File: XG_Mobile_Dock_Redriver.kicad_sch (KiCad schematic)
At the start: 141 parts, among them J1 5-1775443-8, J13 39301240, J14 I2C1, J2 20455-040E-76, J3 20455-040E-76, J5 USB_C_Receptacle, J6 455860005, J7 10147430-113T0LF, SW1 SW_Push, U1 DS320PR810NJXR, U2 DS320PR810NJXR, U6 AT24C02D-PUM

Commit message: stuff
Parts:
- removed R100, R104, R69, R73, R81, R88, R92, R96: 75k, Resistor_SMD:R_0603_1608Metric, symbol Device:R
- removed R102, R105, R108, R67, R71, R98: 8.25k, Resistor_SMD:R_0603_1608Metric, symbol Device:R
- removed R103, R68, R72, R80, R87, R91, R95, R99: 24.9k, Resistor_SMD:R_0603_1608Metric, symbol Device:R
- removed R107, R64, R78, R82, R89, R93: 1k, Resistor_SMD:R_0603_1608Metric, symbol Device:R
- removed R111, R112: 4.7k, Resistor_SMD:R_0402_1005Metric, symbol Device:R
- removed SW10, SW11, SW12, SW13, SW14, SW15, SW6, SW7: ~, DSWB04LHGET:SW-TH_DSWB04LHGET, symbol DSWB04LHGET:DSWB04LHGET
- removed SW16, SW17, SW18, SW19: ~, DSWB01LHGET:SW-TH_DSWB01LHGET, symbol DSWB01LHGET:DSWB01LHGET
- removed SW2, SW3: ~, DSWB03LHGET:SW-TH_DSWB03LHGET, symbol DSWB03LHGET:DSWB03LHGET
- removed U5: ~, DIP-8_L10.2-W10.2-P2.54-LS7.6-BL:DIP-8_L10.2-W10.2-P2.54-LS7.6-BL, symbol DS1009-08AT1NX-0A2:DS1009-08AT1NX-0A2
- removed U6: AT24C02D-PUM, AT24C02D-PUM:PDIP8_300MC_MCH, symbol AT24C02D-PUM:AT24C02D-PUM
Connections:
- net CPU_TO_GPU_EQ0_0: now also R70.2
- net CPU_TO_GPU_EQ0_1: now also R97.2
- net CPU_TO_GPU_EQ1_0: now also R66.2
- net CPU_TO_GPU_EQ1_1: now also R101.2
- net GPU_TO_CPU_EQ0_0: no longer U2.59 (EQ0_0/ADDR0)
- net GPU_TO_CPU_EQ0_1: now also R90.2
- net GPU_TO_CPU_EQ1_0: now also R79.2
- net GPU_TO_CPU_EQ1_1: now also R94.2
- net at U1.61 (MODE): now also R106.2
- net at U2.61 (MODE): now also R109.2
- net at R83.2: now also U2.59 (EQ0_0/ADDR0)
- no-connect marks 4 -> 8
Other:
- moved on the sheet: R101, R106, R109, R66, R70, R79, R83, R90, R94, R97

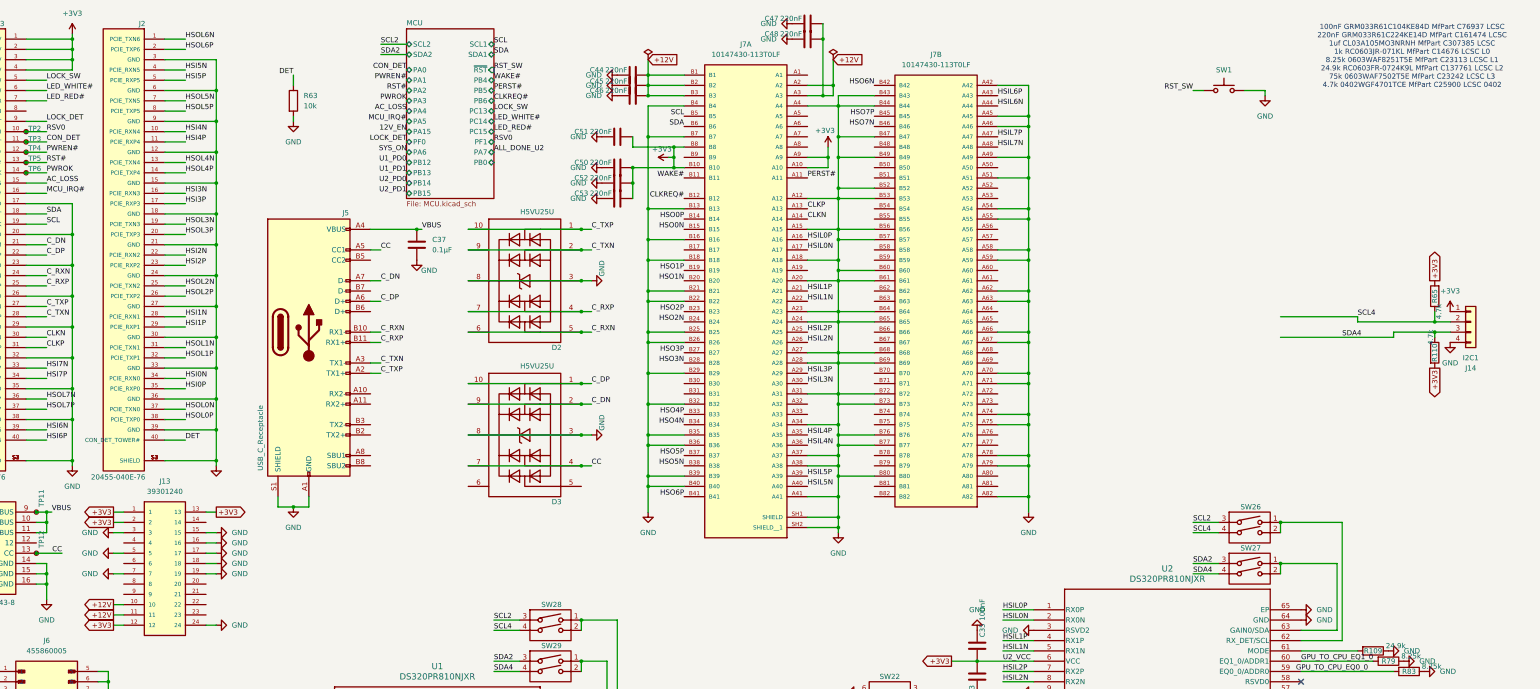
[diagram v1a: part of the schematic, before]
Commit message: added support to control psu from MCU plus standby power for MCU
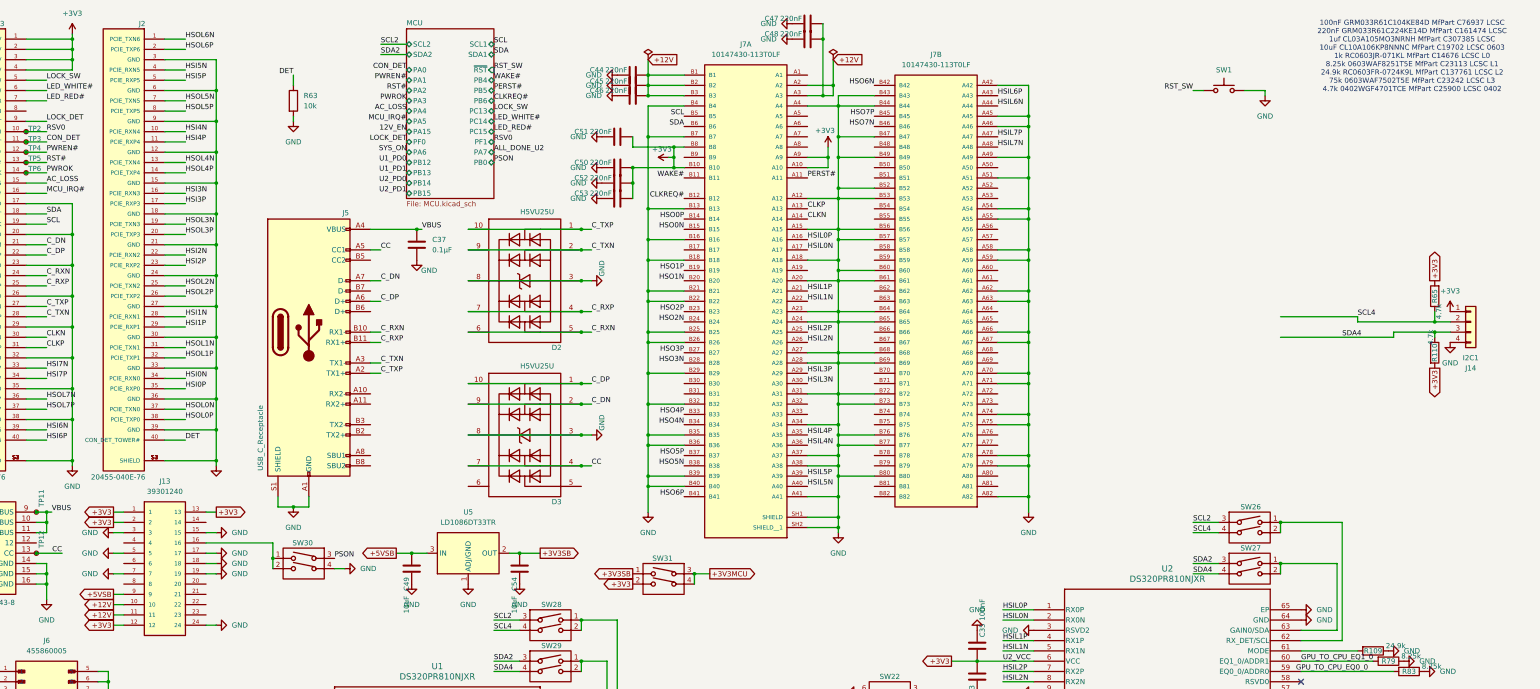
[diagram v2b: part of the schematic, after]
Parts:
- added C49, C54: 10uF, Capacitor_SMD:C_0201_0603Metric, symbol Device:C
- added SW30, SW31: ~, DSWB02LHGET:SW-TH_DSWB02LHGET, symbol DSWB02LHGET:DSWB02LHGET
- added U5: LD1086DT33TR, LD1086DT33TR:TO-252-2_L6.5-W6.1-P4.58-LS10.0-TL, symbol Regulator_Linear:LD1086DT33TR
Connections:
- net +3V3: now also SW31.2
- net GND: now also C49.1, C54.1, SW30.4, U5.1 (ADJ/GND); no longer J13.16
- net +5VSB: now reaches J13.9
- net +5VSB: now also C49.2, U5.3 (IN)
- new net: J13.16, SW30.1, SW30.2
- new net +3V3MCU: SW31.3, SW31.4
- new net +3V3SB: C54.2, SW31.1, U5.2 (OUT)
- new net PSON: SW30.3
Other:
- note added: "100nF GRM033R61C104KE84D MfPart C76937 LCSC 220nF GRM033R61C224KE14D MfPart C161474 LCSC 1uf CL03A105MO3NRNH MfPart C307385 LCSC 10uF CL10A106KP8NNNC MfPart C19702 LCSC 0603 1k RC0603JR-071KL MfPart C14676 LCSC L0 8.25k 0603WAF8251T5E MfPart C23113 LCSC L1 24.9k RC0603FR-0724K9L MfPart C137761 LCSC L2 75k 0603WAF7502T5E MfPart C23242 LCSC L3 4.7k 0402WGF4701TCE MfPart C25900 LCSC 0402"
- note removed: "100nF GRM033R61C104KE84D MfPart C76937 LCSC 220nF GRM033R61C224KE14D MfPart C161474 LCSC 1uf CL03A105MO3NRNH MfPart C307385 LCSC 1k RC0603JR-071KL MfPart C14676 LCSC L0 8.25k 0603WAF8251T5E MfPart C23113 LCSC L1 24.9k RC0603FR-0724K9L MfPart C137761 LCSC L2 75k 0603WAF7502T5E MfPart C23242 LCSC L3 4.7k 0402WGF4701TCE MfPart C25900 LCSC 0402"

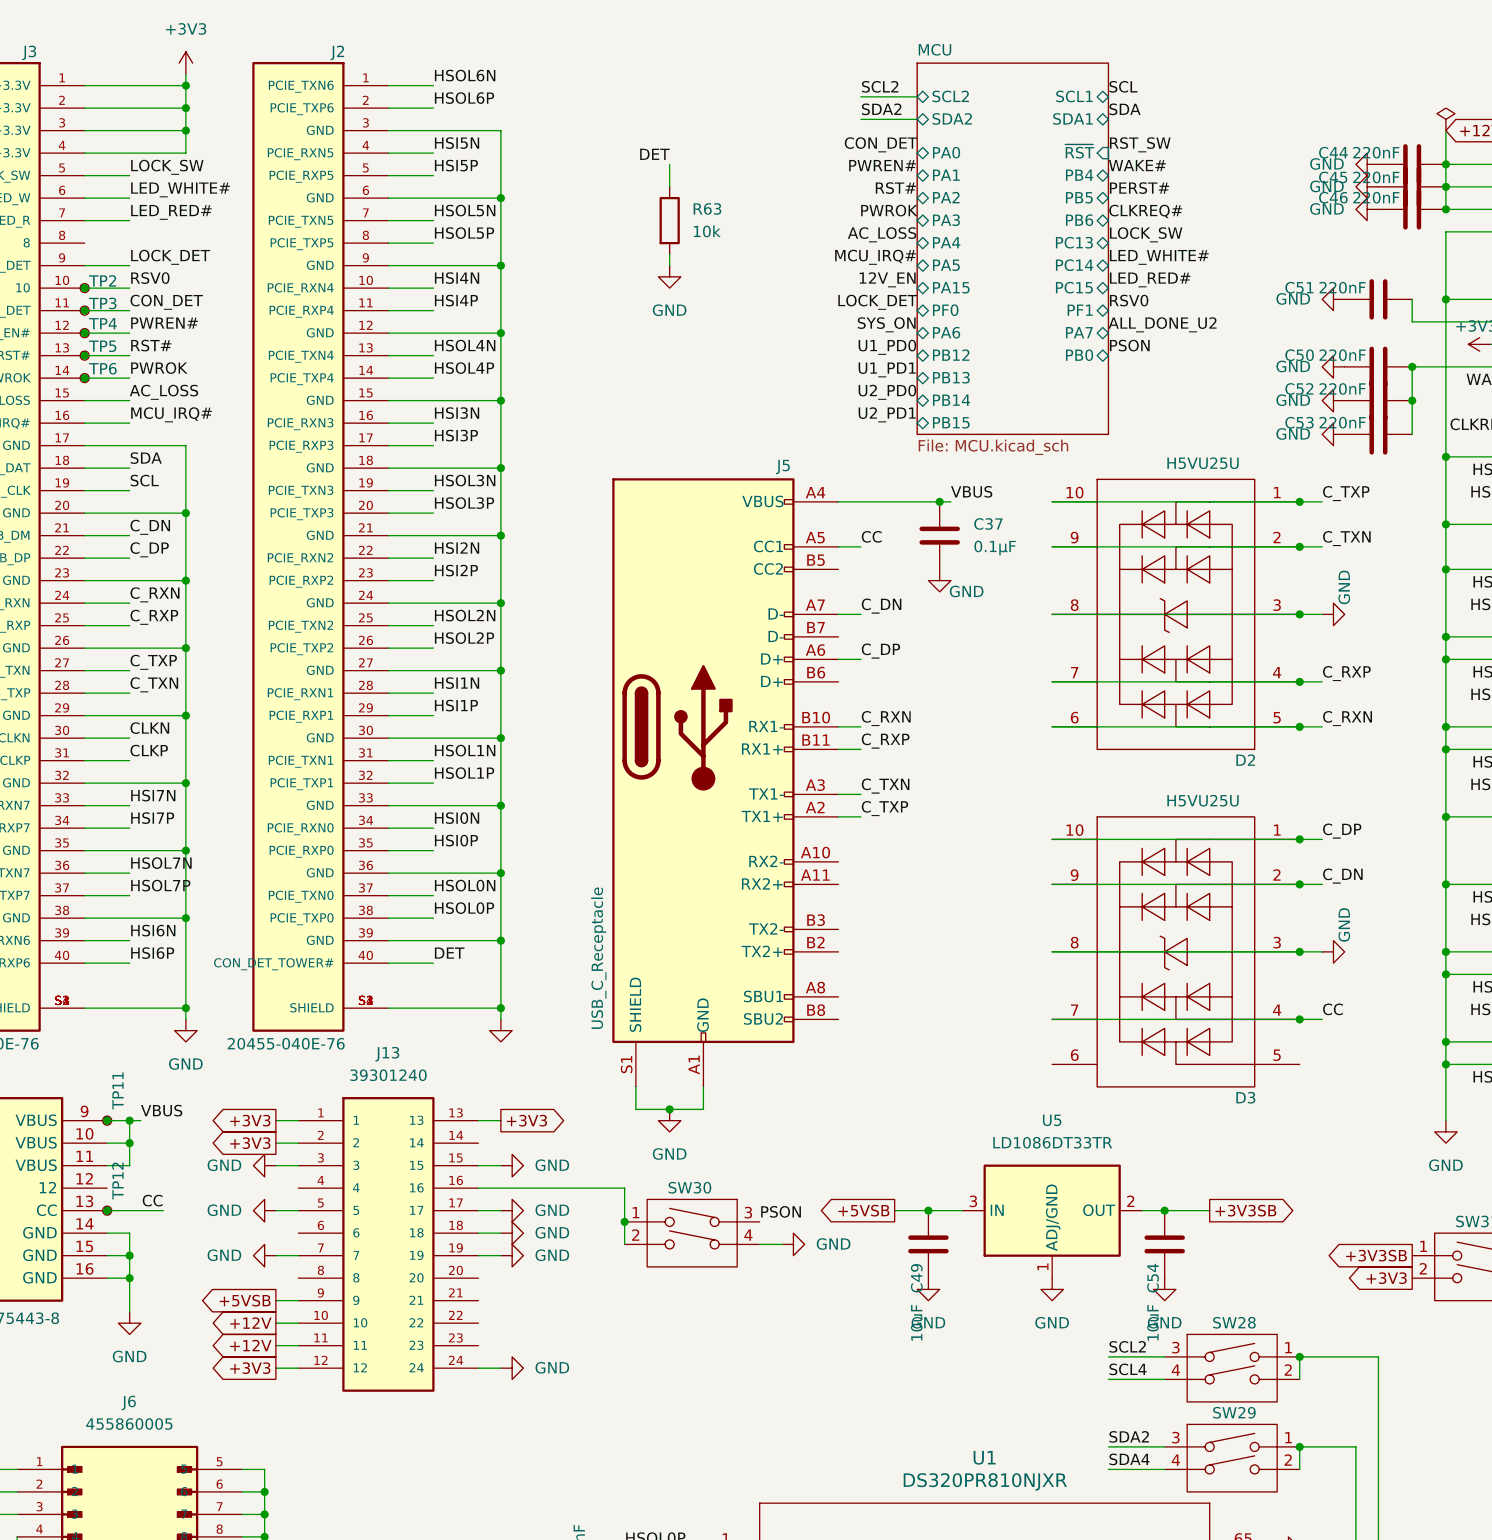
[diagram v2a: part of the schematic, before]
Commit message: added dedicated power to MCU and PSU control from MCU
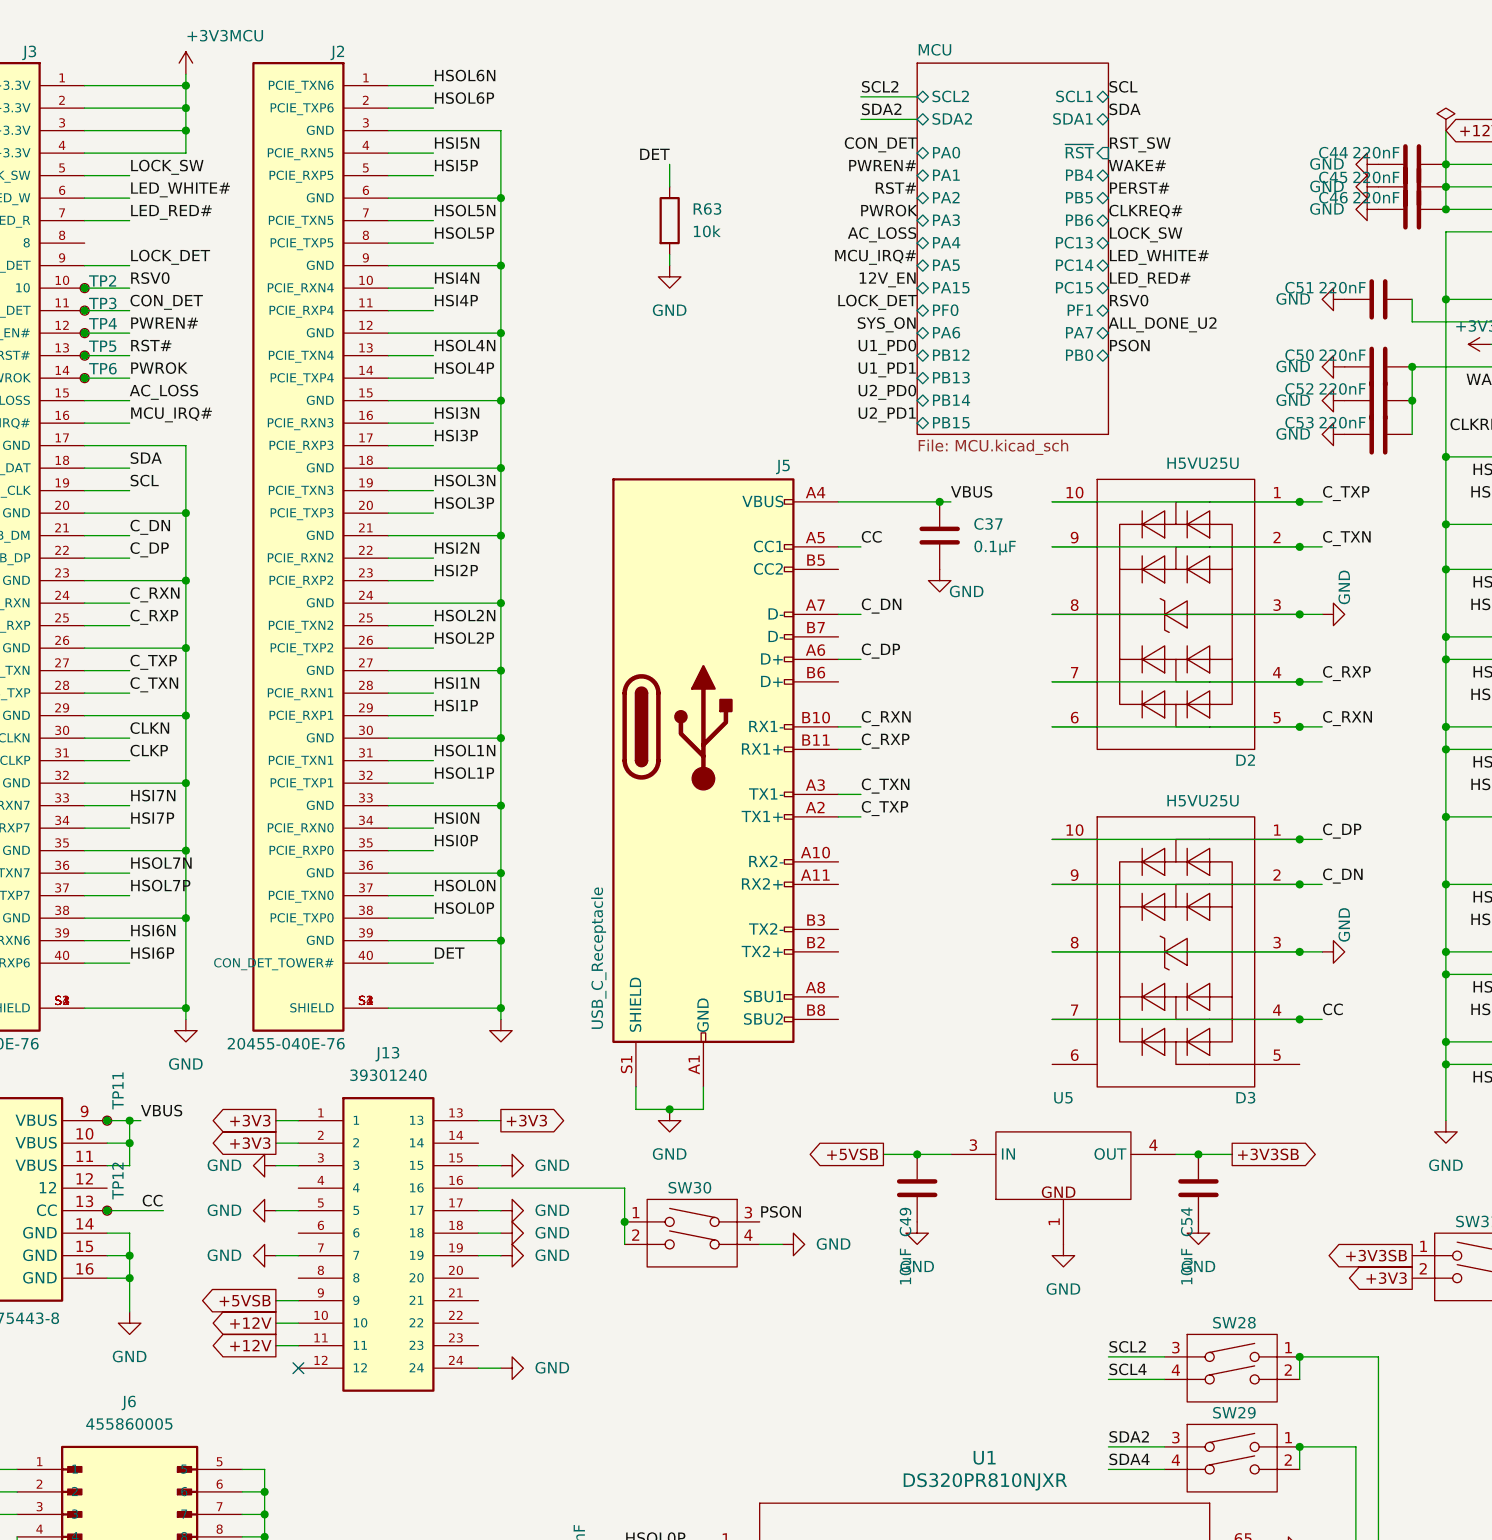
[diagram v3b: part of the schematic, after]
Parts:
- removed U5: LD1086DT33TR, LD1086DT33TR:TO-252-2_L6.5-W6.1-P4.58-LS10.0-TL, symbol Regulator_Linear:LD1086DT33TR
- added U5: ~, LD1086DT33TR:TO-252-2_L6.5-W6.1-P4.58-LS10.0-TL, symbol LD1086DT33TR:LD1086DT33TR
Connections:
- net +3V3: no longer J13.12, J3.1 (+3.3V), J3.2 (+3.3V), J3.3 (+3.3V), J3.4 (+3.3V)
- net +3V3MCU: now also J3.1 (+3.3V), J3.2 (+3.3V), J3.3 (+3.3V), J3.4 (+3.3V)
- net +3V3SB: now also U5.4 (OUT)
- net +5VSB: now also U5.3 (IN)
- net GND: now also U5.1 (GND)
- no-connect marks 8 -> 9
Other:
- moved on the sheet: C49, C54

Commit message: fixed issues
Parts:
- C49, C54: footprint Capacitor_SMD:C_0201_0603Metric -> Capacitor_SMD:C_0603_1608Metric
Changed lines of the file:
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@@
 			)
 		)
-		(property "Footprint" "Capacitor_SMD:C_0201_0603Metric"
+		(property "Footprint" "Capacitor_SMD:C_0603_1608Metric"
 			(at 130.5052 139.7 0)
 			(effects
@@
 			)
 		)
-		(property "Footprint" "Capacitor_SMD:C_0201_0603Metric"
+		(property "Footprint" "Capacitor_SMD:C_0603_1608Metric"
 			(at 162.2552 139.7 0)
 			(effects

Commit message: added new models and cleaned up board
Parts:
- removed SW20, SW21, SW22, SW23: ~, DSWB03LHGET:SW-TH_DSWB03LHGET, symbol DSWB03LHGET:DSWB03LHGET
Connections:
- net GPU_TO_CPU_EQ0_0: now also R83.2, U2.59 (EQ0_0/ADDR0)
- net U1_PD0: now also U1.25 (PD0)
- net U1_PD1: now also U1.26 (PD1)
- net U2_PD0: now also U2.25 (PD0)
- net U2_PD1: now also U2.26 (PD1)

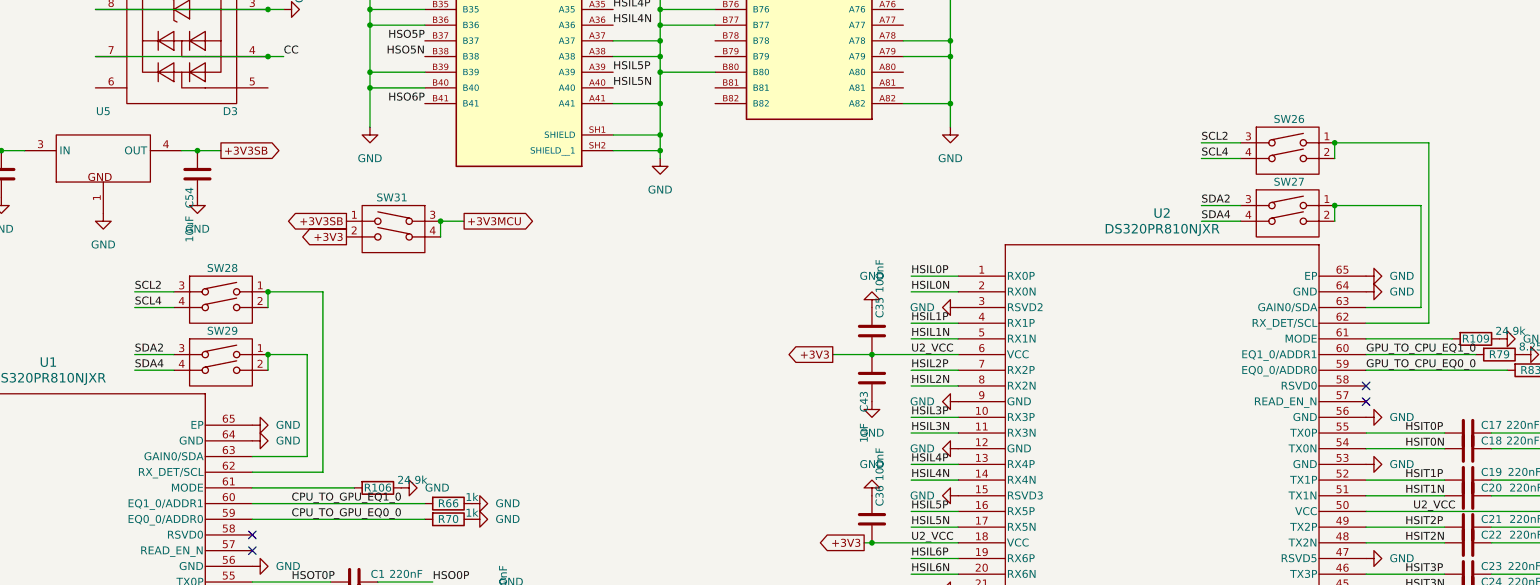
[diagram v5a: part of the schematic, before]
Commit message: added fewer dip switches
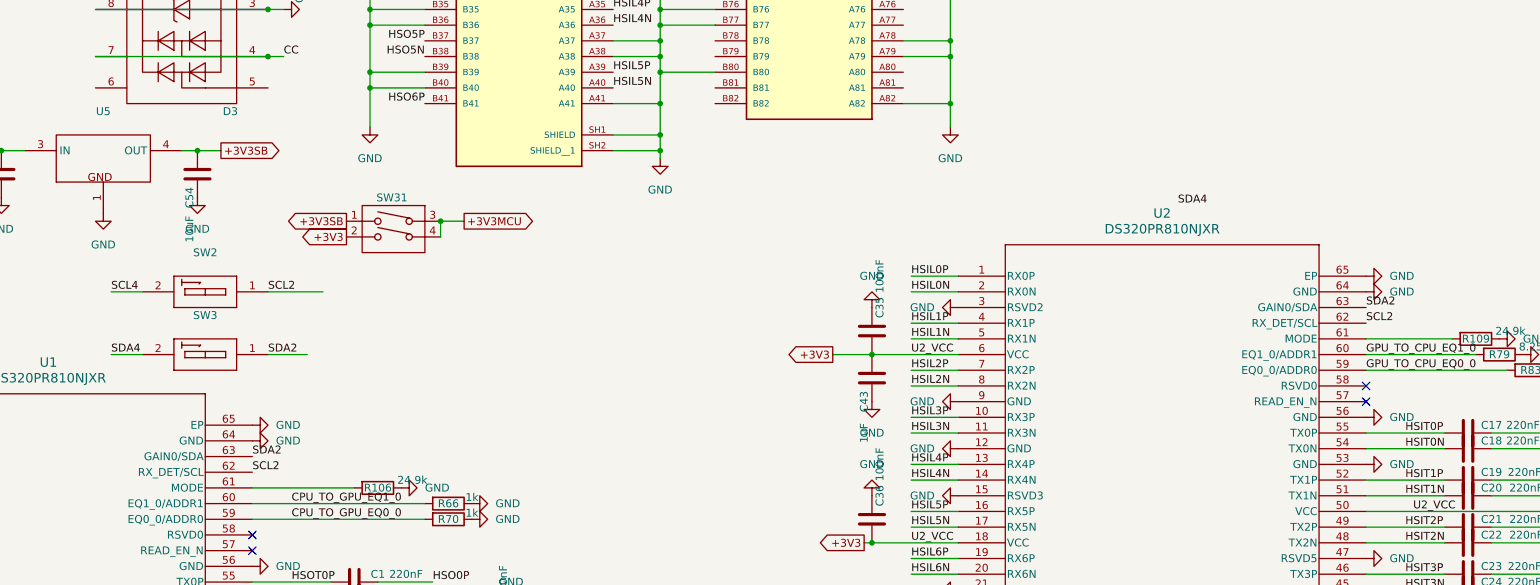
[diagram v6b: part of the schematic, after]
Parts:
- removed SW26, SW27, SW28, SW29: ~, DSWB02LHGET:SW-TH_DSWB02LHGET, symbol DSWB02LHGET:DSWB02LHGET
- added SW2, SW3: ~, DSWB01LHGET:SW-TH_DSWB01LHGET, symbol DSWB01LHGET:DSWB01LHGET
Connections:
- net SCL2: now also U1.62 (RX_DET/SCL), U2.62 (RX_DET/SCL), SW2.1 (A1)
- net SCL4: now also SW2.2
- net SDA2: now also U1.63 (GAIN0/SDA), U2.63 (GAIN0/SDA), SW3.1 (A1)
- net SDA4: now also SW3.2
